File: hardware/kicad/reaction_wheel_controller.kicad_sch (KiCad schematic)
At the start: 0 parts

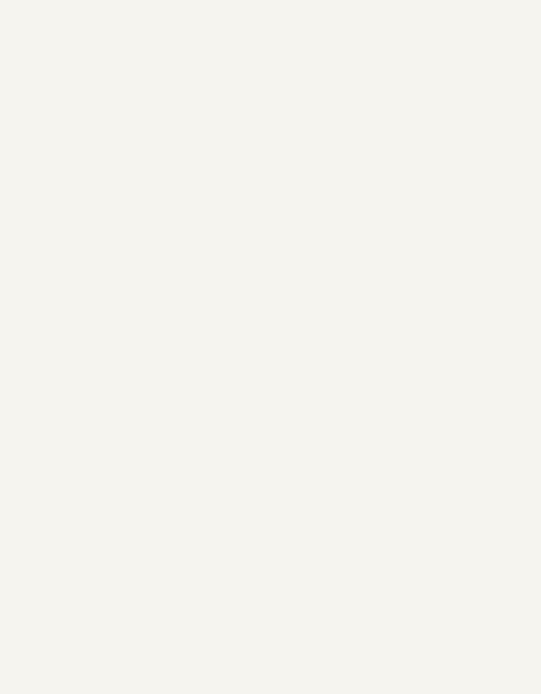
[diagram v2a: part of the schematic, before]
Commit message: hardware: review schematic and align mechanical and probe attributes
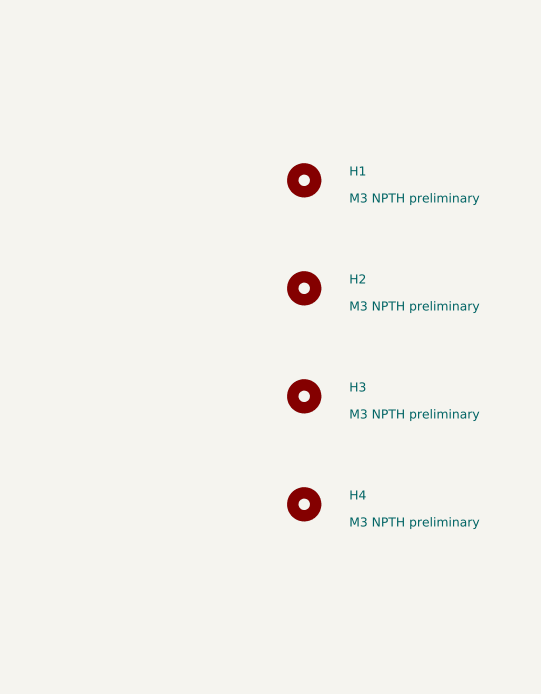
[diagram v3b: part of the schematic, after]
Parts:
- added H1, H2, H3, H4: M3 NPTH preliminary, MountingHole:MountingHole_3.2mm_M3, symbol Mechanical:MountingHole
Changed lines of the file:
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@@
   (title_block
     (title "Reaction Wheel Controller - Concept Blocks")
-    (date "2026-10-02")
-    (rev "0.3")
+    (date "2026-10-03")
+    (rev "0.4")
     (comment 1 "Overview blocks only; electrical implementation on sheets 2-5")
   )
@@
 (sheet (at 93.98 172.72) (size 66.04 10.16) (stroke (width 0.254) (type default)) (fill (color 0 0 0 0)) (property "Sheetname" "ENCODER ESC" (at 93.98 171.45 0) (effects (font (size 1 1)) (justify left bottom))) (property "Sheetfile" "encoder_esc.kicad_sch" (at 93.98 184.15 0) (effects (font (size 1 1)) (justify left top))) (instances (project "reaction_wheel_controller" (path "/56c7795e-d739-4c45-a73e-6c5ecdfd94b9" (page "4")))))
 (sheet (at 172.72 172.72) (size 66.04 10.16) (stroke (width 0.254) (type default)) (fill (color 0 0 0 0)) (property "Sheetname" "UART" (at 172.72 171.45 0) (effects (font (size 1 1)) (justify left bottom))) (property "Sheetfile" "uart_interfaces.kicad_sch" (at 172.72 184.15 0) (effects (font (size 1 1)) (justify left top))) (instances (project "reaction_wheel_controller" (path "/56c7795e-d739-4c45-a73e-6c5ecdfd94b9" (page "5")))))
+(symbol (lib_id "Mechanical:MountingHole") (at 340 62 0) (unit 1) (in_bom no) (on_board yes) (dnp no) (property "Reference" "H1" (at 345 61 0) (effects (font (size 1 1)) (justify left))) (property "Value" "M3 NPTH preliminary" (at 345 64 0) (effects (font (size 1 1)) (justify left))) (property "Footprint" "MountingHole:MountingHole_3.2mm_M3" (at 340 62 0) (effects (font (size 1 1)) (hide yes))) (instances (project "reaction_wheel_controller" (path "/56c7795e-d739-4c45-a73e-6c5ecdfd94b9" (reference "H1") (unit 1)))))
+(symbol (lib_id "Mechanical:MountingHole") (at 340 74 0) (unit 1) (in_bom no) (on_board yes) (dnp no) (property "Reference" "H2" (at 345 73 0) (effects (font (size 1 1)) (justify left))) (property "Value" "M3 NPTH preliminary" (at 345 76 0) (effects (font (size 1 1)) (justify left))) (property "Footprint" "MountingHole:MountingHole_3.2mm_M3" (at 340 74 0) (effects (font (size 1 1)) (hide yes))) (instances (project "reaction_wheel_controller" (path "/56c7795e-d739-4c45-a73e-6c5ecdfd94b9" (reference "H2") (unit 1)))))
+(symbol (lib_id "Mechanical:MountingHole") (at 340 86 0) (unit 1) (in_bom no) (on_board yes) (dnp no) (property "Reference" "H3" (at 345 85 0) (effects (font (size 1 1)) (justify left))) (property "Value" "M3 NPTH preliminary" (at 345 88 0) (effects (font (size 1 1)) (justify left))) (property "Footprint" "MountingHole:MountingHole_3.2mm_M3" (at 340 86 0) (effects (font (size 1 1)) (hide yes))) (instances (project "reaction_wheel_controller" (path "/56c7795e-d739-4c45-a73e-6c5ecdfd94b9" (reference "H3") (unit 1)))))
+(symbol (lib_id "Mechanical:MountingHole") (at 340 98 0) (unit 1) (in_bom no) (on_board yes) (dnp no) (property "Reference" "H4" (at 345 97 0) (effects (font (size 1 1)) (justify left))) (property "Value" "M3 NPTH preliminary" (at 345 100 0) (effects (font (size 1 1)) (justify left))) (property "Footprint" "MountingHole:MountingHole_3.2mm_M3" (at 340 98 0) (effects (font (size 1 1)) (hide yes))) (instances (project "reaction_wheel_controller" (path "/56c7795e-d739-4c45-a73e-6c5ecdfd94b9" (reference "H4") (unit 1)))))
 )
